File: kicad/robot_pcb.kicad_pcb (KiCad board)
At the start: 2 copper layers, 65.4 x 66 mm, 31 parts, among them J1 Conn_01x19_Female, J2 Conn_01x19_Female, J3 esp32 cam, J4 motor1, J5 motor2, J6 motor pwr, J7 esp32 pwr, Q1 Q_PMOS_GDS, Q2 Q_NMOS_GDS, Q3 Q_PMOS_GDS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

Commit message: add measurements kicad
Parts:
- moved J5 12.1 mm to (149.9, 76.8)
- moved Q7 12.1 mm to (144.8, 94.6)
- moved R1 12.1 mm to (106.7, 76.8)
- moved R2 12.1 mm to (104.2, 76.8)
- moved R5 12.1 mm to (142.2, 76.8)
- moved R6 12.1 mm to (144.8, 76.8)
- moved J4 12.1 mm to (99.1, 76.8)
- moved Q3 12.1 mm to (104.1, 94.6)
- moved J2 12.1 mm to (135.8, 55.2)
- moved Q5 12.1 mm to (144.8, 55.2)
- moved Q1 12.1 mm to (104.1, 55.2)
- moved Q6 12.1 mm to (144.8, 61.6)
- moved Q8 12.1 mm to (144.8, 101.0)
- moved R4 12.1 mm to (106.7, 79.4)
- moved R7 12.1 mm to (144.8, 79.4)
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
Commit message: pcb rev 2
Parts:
- Q1, Q3, Q5, Q7: value Q_PMOS_GDS -> AO3401A; footprint Downloads:SOIC127P490X600X175-8N -> digikey-footprints:SOT-23-3
- Q2, Q4, Q6, Q8: value Q_NMOS_GDS -> IRLML6344TRPBF; footprint Downloads:SOIC127P490X600X175-8N -> digikey-footprints:SOT-23-3
- R1, R2, R3, R4, R5, R6, R7, R8: footprint Resistor_SMD:R_0201_0603Metric_Pad0.64x0.40mm_HandSolder -> Resistor_SMD:R_0805_2012Metric_Pad1.20x1.40mm_HandSolder
- moved R6 27.6 mm to (143.8, 49.3)
- moved R7 15.1 mm to (145.8, 94.5)
- moved R3 15.1 mm to (104.6, 94.5)
- moved R2 14.9 mm to (105.2, 62.0), turned to 0 degrees
- moved U1 9.70 mm to (107.9, 70.6), turned to 180 degrees
- moved Q7 7.18 mm to (149.9, 99.7)
- moved J7 6.61 mm to (106.4, 107.2)
- moved U2 5.94 mm to (106.7, 83.6), turned to -90 degrees
- moved Q3 5.72 mm to (107.7, 99.1), turned to -90 degrees
- moved U3 5.20 mm to (142.3, 71.9), turned to 90 degrees
- moved Q1 4.96 mm to (108.0, 58.4)
- moved Q2 4.07 mm to (101.6, 58.4)
- moved J4 2.79 mm to (101.6, 75.7)
- moved Q4 2.71 mm to (102.2, 99.1), turned to -90 degrees
- moved Q8 2.29 mm to (142.9, 99.7), turned to 0 degrees
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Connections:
- Q1 pad 2: MO1 -> /Vm
- Q1 pad 3: /Vm -> MO1
- Q2 pad 2: MO1 -> MGND
- Q2 pad 3: MGND -> MO1
- Q3 pad 2: MO2 -> /Vm
- Q3 pad 3: /Vm -> MO2
- Q4 pad 2: MO2 -> MGND
- Q4 pad 3: MGND -> MO2
- Q5 pad 2: MO3 -> /Vm
- Q5 pad 3: /Vm -> MO3
- Q6 pad 2: MO3 -> MGND
- Q6 pad 3: MGND -> MO3
- Q7 pad 2: MO4 -> /Vm
- Q7 pad 3: /Vm -> MO4
- Q8 pad 2: MO4 -> MGND
- Q8 pad 3: MGND -> MO4
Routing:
- net /Vm: track 138.7 -> 181.8 mm
- net ESP_GND: track 173.0 -> 148.2 mm
- net /Gate2: track 39.2 -> 15.3 mm, vias 1 -> 2
- net /Gate3: track 33.8 -> 17.3 mm, vias 4 -> 0
- net Net-(R1-Pad1): track 17.9 -> 3.60 mm, vias 2 -> 0
- net MO3: track 25.8 -> 39.0 mm
- net MGND: track 162.0 -> 173.4 mm, vias 5 -> 4
- net Net-(R4-Pad1): track 13.2 -> 3.33 mm
- net Net-(R5-Pad1): track 11.9 -> 3.33 mm
- net MO4: track 30.3 -> 37.8 mm
- net /Gate1: track 23.5 -> 18.6 mm
- net /Vcc: track 6.34 -> 10.7 mm
- net M21: track 7.58 -> 5.27 mm
- net MO1: track 32.2 -> 30.2 mm, vias 3 -> 2
- net MO2: track 29.5 -> 31.4 mm
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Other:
- board size 65.4 x 66 mm -> 65.4 x 67.1 mm
- board text added: "Robot Controller Rev 2"
- board text removed: "RC Robot Controller Rev 1"

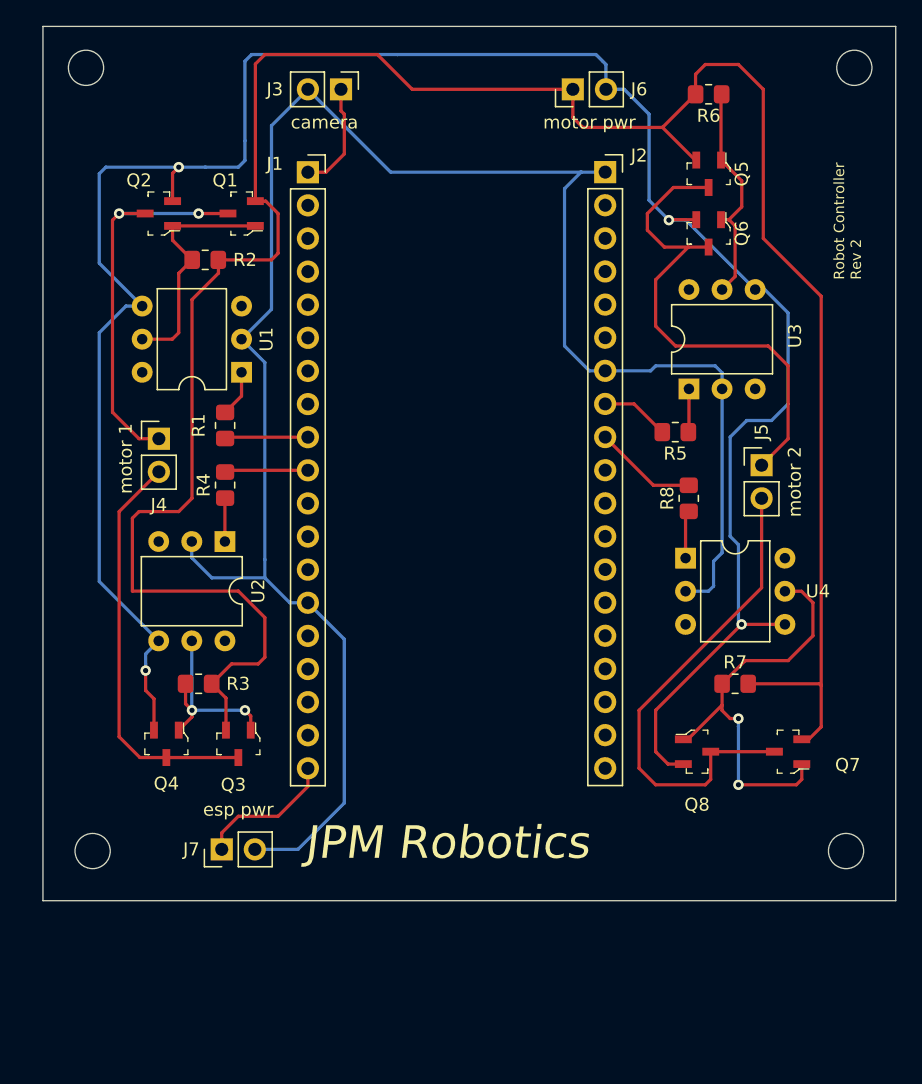
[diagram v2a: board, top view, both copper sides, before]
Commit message: sent out fab for rev2 pcb
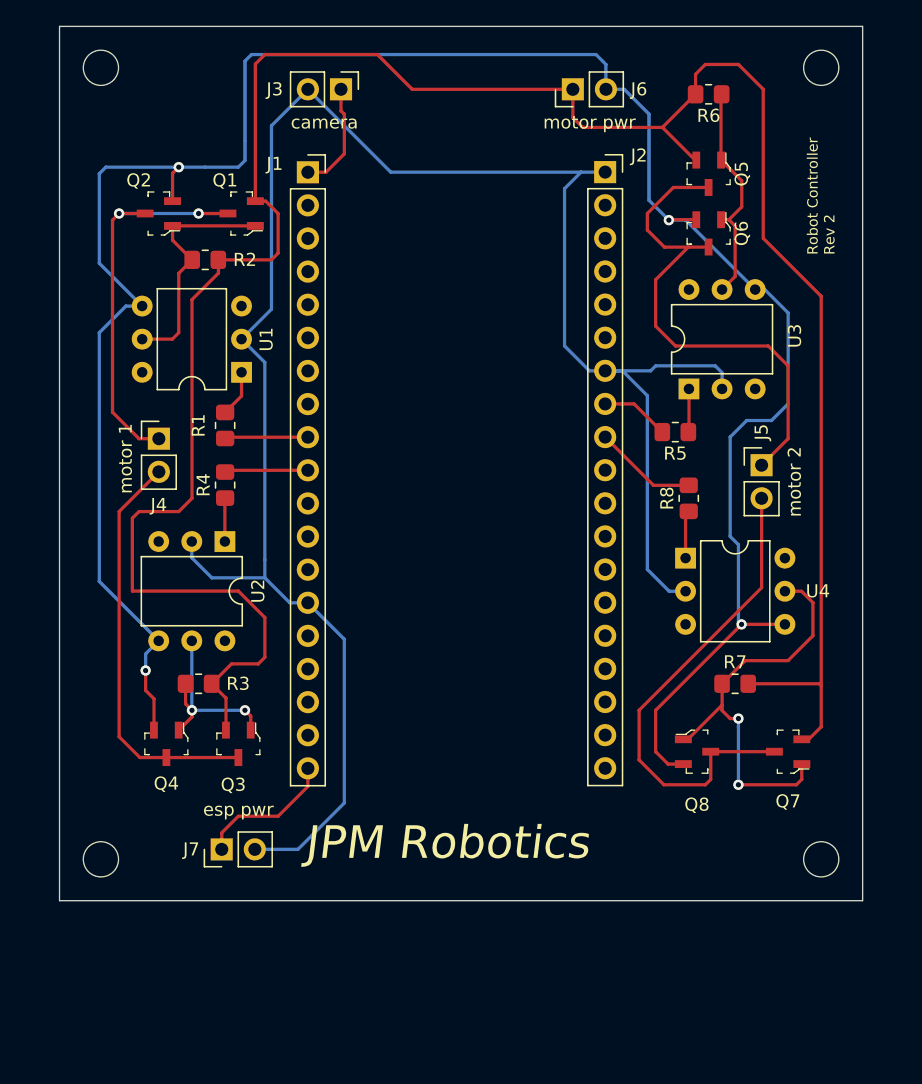
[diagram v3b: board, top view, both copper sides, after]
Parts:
- moved REF4 2.54 mm to (152.4, 47.2)
- moved REF3 2.01 mm to (152.4, 108.0)
- moved REF1 1.14 mm to (97.2, 47.2)
- moved REF2 0.90 mm to (97.2, 108.0)
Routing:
- net ESP_GND: track 148.2 -> 151.5 mm
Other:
- board size 65.4 x 67.1 mm -> 61.6 x 67.1 mm
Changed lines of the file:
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@@
   )
   (footprint "MountingHole:MountingHole_2.7mm_M2.5" (layer "F.Cu")
-    (at 96.012 47.244)
+    (at 97.155 47.244)
     (descr "Mounting Hole 2.7mm, no annular, M2.5")
     (tags "mounting hole 2.7mm no annular m2.5")
@@
     (property "Status" "Active")
     (attr smd)
-    (fp_text reference "Q7" (at -4.572 -1.016) (layer "F.SilkS")
+    (fp_text reference "Q7" (at 0 -3.81) (layer "F.SilkS")
       (effects (font (size 1 1) (thickness 0.15)))
     )
@@
   )
   (footprint "MountingHole:MountingHole_2.7mm_M2.5" (layer "F.Cu")
-    (at 154.94 47.244)
+    (at 152.4 47.244)
     (descr "Mounting Hole 2.7mm, no annular, M2.5")
     (tags "mounting hole 2.7mm no annular m2.5")
@@
   )
   (footprint "MountingHole:MountingHole_2.7mm_M2.5" (layer "F.Cu")
-    (at 96.52 107.315)
+    (at 97.155 107.95)
     (descr "Mounting Hole 2.7mm, no annular, M2.5")
     (tags "mounting hole 2.7mm no annular m2.5")
@@
   )
   (footprint "MountingHole:MountingHole_2.7mm_M2.5" (layer "F.Cu")
-    (at 154.305 107.315)
+    (at 152.4 107.95)
     (descr "Mounting Hole 2.7mm, no annular, M2.5")
     (tags "mounting hole 2.7mm no annular m2.5")
@@
     )
   )
-  (gr_rect (start 158.115 111.125) (end 92.71 44.069) (layer "Edge.Cuts") (width 0.05) (fill none))
+  (gr_rect (start 155.575 111.125) (end 93.98 44.069) (layer "Edge.Cuts") (width 0.05) (fill none))
   (gr_text "motor 1" (at 99.06 77.216 -270) (layer "F.SilkS")
     (effects (font (size 1 1) (thickness 0.15)))
@@
     (effects (font (size 1 1) (thickness 0.15)))
   )
-  (gr_text "Robot Controller\nRev 2" (at 154.432 63.5 -270) (layer "F.SilkS")
+  (gr_text "Robot Controller\nRev 2" (at 152.4 61.595 -270) (layer "F.SilkS")
     (effects (font (size 0.8 0.8) (thickness 0.15)) (justify left))
   )
@@
   (segment (start 113.03 102.362) (end 113.03 100.975) (width 0.25) (layer "F.Cu") (net 32))
   (segment (start 110.744 104.648) (end 113.03 102.362) (width 0.25) (layer "F.Cu") (net 32))
-  (segment (start 141.996 87.391) (end 143.749 87.391) (width 0.25) (layer "B.Cu") (net 44))
   (segment (start 133.985 55.245) (end 135.83 55.245) (width 0.25) (layer "B.Cu") (net 44))
   (segment (start 119.38 55.245) (end 133.985 55.245) (width 0.25) (layer "B.Cu") (net 44))
   (segment (start 108.961 107.188) (end 112.268 107.188) (width 0.25) (layer "B.Cu") (net 44))
-  (segment (start 144.145 86.995) (end 144.145 85.09) (width 0.25) (layer "B.Cu") (net 44))
   (segment (start 111.643 88.275) (end 109.728 86.36) (width 0.25) (layer "B.Cu") (net 44))
   (segment (start 139.319 70.485) (end 135.83 70.485) (width 0.25) (layer "B.Cu") (net 44))
   (segment (start 134.62 70.485) (end 132.715 68.58) (width 0.25) (layer "B.Cu") (net 44))
   (segment (start 144.272 70.104) (end 139.7 70.104) (width 0.25) (layer "B.Cu") (net 44))
-  (segment (start 143.749 87.391) (end 144.145 86.995) (width 0.25) (layer "B.Cu") (net 44))
   (segment (start 105.664 86.36) (end 104.125 84.821) (width 0.25) (layer "B.Cu") (net 44))
+  (segment (start 137.16 70.485) (end 139.065 72.39) (width 0.25) (layer "B.Cu") (net 44))
   (segment (start 107.94 68.057) (end 109.728 69.845) (width 0.25) (layer "B.Cu") (net 44))
   (segment (start 144.795 70.627) (end 144.272 70.104) (width 0.25) (layer "B.Cu") (net 44))
   (segment (start 132.715 68.58) (end 132.715 56.515) (width 0.25) (layer "B.Cu") (net 44))
-  (segment (start 144.795 84.44) (end 144.795 71.872) (width 0.25) (layer "B.Cu") (net 44))
   (segment (start 104.125 84.821) (end 104.125 83.576) (width 0.25) (layer "B.Cu") (net 44))
   (segment (start 109.728 84.973) (end 109.728 86.36) (width 0.25) (layer "B.Cu") (net 44))
   (segment (start 115.824 103.632) (end 115.824 91.069) (width 0.25) (layer "B.Cu") (net 44))
   (segment (start 109.728 86.36) (end 105.664 86.36) (width 0.25) (layer "B.Cu") (net 44))
+  (segment (start 139.065 72.39) (end 139.065 85.725) (width 0.25) (layer "B.Cu") (net 44))
+  (segment (start 135.83 70.485) (end 137.16 70.485) (width 0.25) (layer "B.Cu") (net 44))
   (segment (start 144.795 71.872) (end 144.795 70.627) (width 0.25) (layer "B.Cu") (net 44))
   (segment (start 113.03 48.895) (end 119.38 55.245) (width 0.25) (layer "B.Cu") (net 44))
@@
   (segment (start 135.83 70.485) (end 134.62 70.485) (width 0.25) (layer "B.Cu") (net 44))
   (segment (start 107.94 68.057) (end 110.236 65.761) (width 0.25) (layer "B.Cu") (net 44))
-  (segment (start 144.145 85.09) (end 144.795 84.44) (width 0.25) (layer "B.Cu") (net 44))
   (segment (start 139.7 70.104) (end 139.319 70.485) (width 0.25) (layer "B.Cu") (net 44))
+  (segment (start 139.065 85.725) (end 140.731 87.391) (width 0.25) (layer "B.Cu") (net 44))
   (segment (start 110.236 51.689) (end 113.03 48.895) (width 0.25) (layer "B.Cu") (net 44))
   (segment (start 112.268 107.188) (end 115.824 103.632) (width 0.25) (layer "B.Cu") (net 44))
   (segment (start 109.728 69.845) (end 109.728 84.973) (width 0.25) (layer "B.Cu") (net 44))
+  (segment (start 140.731 87.391) (end 141.996 87.391) (width 0.25) (layer "B.Cu") (net 44))
   (segment (start 115.824 91.069) (end 113.03 88.275) (width 0.25) (layer "B.Cu") (net 44))
   (segment (start 106.665 80.263) (end 106.665 83.576) (width 0.25) (layer "F.Cu") (net 47))
@@
   (segment (start 142.206 60.994) (end 143.764 60.994) (width 0.25) (layer "F.Cu") (net 50))
   (segment (start 139.065 59.69) (end 139.065 58.42) (width 0.25) (layer "F.Cu") (net 50))
-  (segment (start 138.43 100.965) (end 139.7 102.235) (width 0.25) (layer "F.Cu") (net 51))
-  (segment (start 138.43 96.52) (end 138.43 100.965) (width 0.25) (layer "F.Cu") (net 51))
+  (segment (start 143.925 101.82) (end 143.925 99.695) (width 0.25) (layer "F.Cu") (net 51))
+  (segment (start 138.43 96.52) (end 138.43 100.33) (width 0.25) (layer "F.Cu") (net 51))
+  (segment (start 147.828 80.264) (end 147.828 87.122) (width 0.25) (layer "F.Cu") (net 51))
+  (segment (start 140.335 102.235) (end 143.51 102.235) (width 0.25) (layer "F.Cu") (net 51))
+  (segment (start 143.925 99.695) (end 148.81 99.695) (width 0.25) (layer "F.Cu") (net 51))
+  (segment (start 138.43 100.33) (end 140.335 102.235) (width 0.25) (layer "F.Cu") (net 51))
   (segment (start 147.828 87.122) (end 138.43 96.52) (width 0.25) (layer "F.Cu") (net 51))
-  (segment (start 143.925 99.695) (end 148.81 99.695) (width 0.25) (layer "F.Cu") (net 51))
-  (segment (start 143.925 101.82) (end 143.51 102.235) (width 0.25) (layer "F.Cu") (net 51))
-  (segment (start 147.828 80.264) (end 147.828 87.122) (width 0.25) (layer "F.Cu") (net 51))
-  (segment (start 143.925 99.695) (end 143.925 101.82) (width 0.25) (layer "F.Cu") (net 51))
-  (segment (start 143.51 102.235) (end 139.7 102.235) (width 0.25) (layer "F.Cu") (net 51))
+  (segment (start 143.51 102.235) (end 143.925 101.82) (width 0.25) (layer "F.Cu") (net 51))
   (segment (start 139.7 96.52) (end 139.7 99.695) (width 0.25) (layer "F.Cu") (net 54))
   (segment (start 102.65 55.338) (end 102.65 57.47) (width 0.25) (layer "F.Cu") (net 54))

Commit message: add measurements
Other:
- board text added: "JPM ROBOTICS"
- board text added: "RC ROBOT PCB LAYOUT"
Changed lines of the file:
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@@
     (thickness 1.6)
   )
-  (paper "A4")
+  (paper "User" 210.007 200)
   (layers
     (0 "F.Cu" signal)
@@
     (effects (font (size 1 1) (thickness 0.15)))
   )
+  (gr_text "RC ROBOT PCB LAYOUT" (at 118.11 179.705) (layer "Cmts.User")
+    (effects (font (size 1 1) (thickness 0.15)))
+  )
+  (gr_text "JPM ROBOTICS" (at 144.78 164.465) (layer "Cmts.User")
+    (effects (font (size 5 5) (thickness 1)))
+  )
+  (dimension (type aligned) (layer "Cmts.User")
+    (pts (xy 111.76 71.12) (xy 137.16 71.12))
+    (height 3.174999)
+    (gr_text "25.4000 mm" (at 124.46 73.144999) (layer "Cmts.User")
+      (effects (font (size 1 1) (thickness 0.15)))
+    )
+    (format (units 3) (units_format 1) (precision 4))
+    (style (thickness 0.1) (arrow_length 1.27) (text_position_mode 0) (extension_height 0.58642) (extension_offset 0.5) keep_text_aligned)
+  )
+  (dimension (type aligned) (layer "Cmts.User")
+    (pts (xy 97.155 107.95) (xy 152.4 107.95))
+    (height 10.795)
+    (gr_text "55.2450 mm" (at 124.7775 117.595) (layer "Cmts.User")
+      (effects (font (size 1 1) (thickness 0.15)))
+    )
+    (format (units 3) (units_format 1) (precision 4))
+    (style (thickness 0.1) (arrow_length 1.27) (text_position_mode 0) (extension_height 0.58642) (extension_offset 0.5) keep_text_aligned)
+  )
+  (dimension (type aligned) (layer "Cmts.User")
+    (pts (xy 155.575 111.125) (xy 155.575 44.069))
+    (height 8.89)
+    (gr_text "67.0560 mm" (at 163.315 77.597 90) (layer "Cmts.User")
+      (effects (font (size 1 1) (thickness 0.15)))
+    )
+    (format (units 3) (units_format 1) (precision 4))
+    (style (thickness 0.1) (arrow_length 1.27) (text_position_mode 0) (extension_height 0.58642) (extension_offset 0.5) keep_text_aligned)
+  )
+  (dimension (type aligned) (layer "Cmts.User")
+    (pts (xy 93.98 111.125) (xy 155.575 111.125))
+    (height 12.065)
+    (gr_text "61.5950 mm" (at 124.7775 122.04) (layer "Cmts.User")
+      (effects (font (size 1 1) (thickness 0.15)))
+    )
+    (format (units 3) (units_format 1) (precision 4))
+    (style (thickness 0.1) (arrow_length 1.27) (text_position_mode 0) (extension_height 0.58642) (extension_offset 0.5) keep_text_aligned)
+  )
   (segment (start 106.68 73.676) (end 107.94 72.416) (width 0.25) (layer "F.Cu") (net 1))
